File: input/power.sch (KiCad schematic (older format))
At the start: 61 parts, among them Q2 2STD1665T4, Q3 NSS1C300ET4G, U4 OPA830, U6 OPA830, U7 MCP1755S-3302E/DB, U8 NCP1117STAT3G

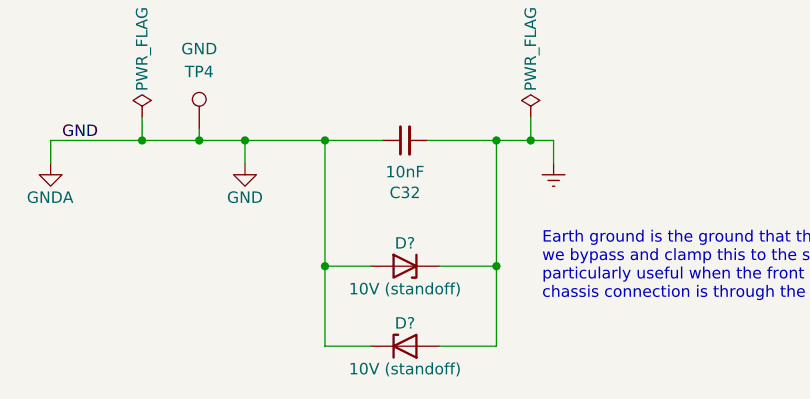
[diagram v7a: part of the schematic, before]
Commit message: Fix to swapped opamp pins in reference_buffer.sch, assigned opamp type, annotated.  Improved comments. Other changes are almost entirely kicad inflicted spurious modifications of multi-instance sub-sheets.
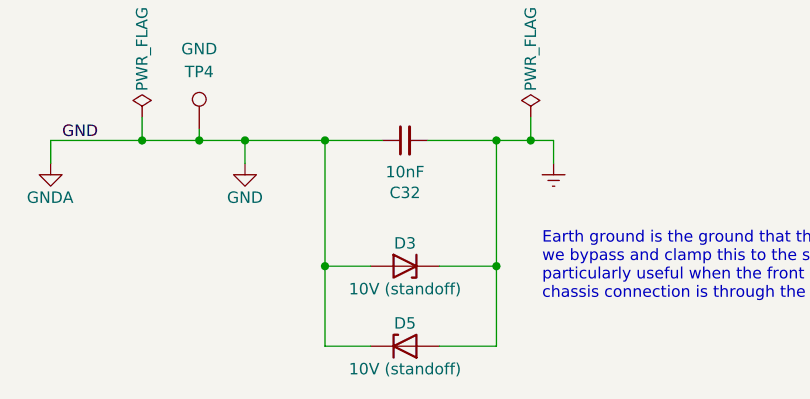
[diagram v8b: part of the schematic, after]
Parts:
- gave numbers to parts that had none: 2
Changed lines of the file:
@@
 	4350 1400 4500 1400
 $Comp
-L Device:D_Zener D?
+L Device:D_Zener D3
 U 1 1 5FA1D797
 P 3650 8900
-AR Path="/5E51E83D/5FA1D797" Ref="D?"  Part="1"
+AR Path="/5E51E83D/5FA1D797" Ref="D3"  Part="1"
 AR Path="/5E1D6729/5FA1D797" Ref="D?"  Part="1"
 AR Path="/5E624B3C/5E51E83D/5FA1D797" Ref="D?"  Part="1"
 AR Path="/5E62FD57/5E630FEC/5FA1D797" Ref="D?"  Part="1"
-F 0 "D?" H 3650 8800 50  0000 C CNN
+F 0 "D3" H 3650 8800 50  0000 C CNN
 F 1 "10V (standoff)" H 3650 9000 50  0000 C CNN
 F 2 "Diode_SMD:D_SMA" H 3650 8900 50  0001 C CNN
@@
 	2500 8350 2750 8350
 $Comp
-L Device:D_Zener D?
+L Device:D_Zener D5
 U 1 1 5FA3410D
 P 3650 9250
-AR Path="/5E51E83D/5FA3410D" Ref="D?"  Part="1"
+AR Path="/5E51E83D/5FA3410D" Ref="D5"  Part="1"
 AR Path="/5E1D6729/5FA3410D" Ref="D?"  Part="1"
 AR Path="/5E624B3C/5E51E83D/5FA3410D" Ref="D?"  Part="1"
 AR Path="/5E62FD57/5E630FEC/5FA3410D" Ref="D?"  Part="1"
-F 0 "D?" H 3650 9350 50  0000 C CNN
+F 0 "D5" H 3650 9350 50  0000 C CNN
 F 1 "10V (standoff)" H 3650 9150 50  0000 C CNN
 F 2 "Diode_SMD:D_SMA" H 3650 9250 50  0001 C CNN
